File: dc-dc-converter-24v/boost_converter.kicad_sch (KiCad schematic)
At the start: 44 parts, among them Q1 SQJA42EP, Q2 SQJA42EP, Q3 SQJA42EP, Q4 SQJA42EP, U1 LM5176

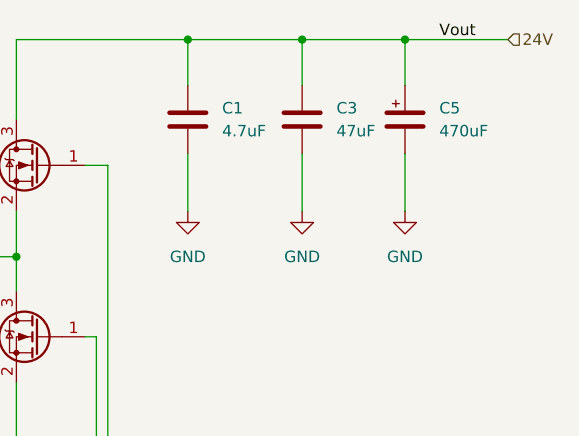
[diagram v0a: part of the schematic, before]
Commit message: improve output filter of DC-DC converter
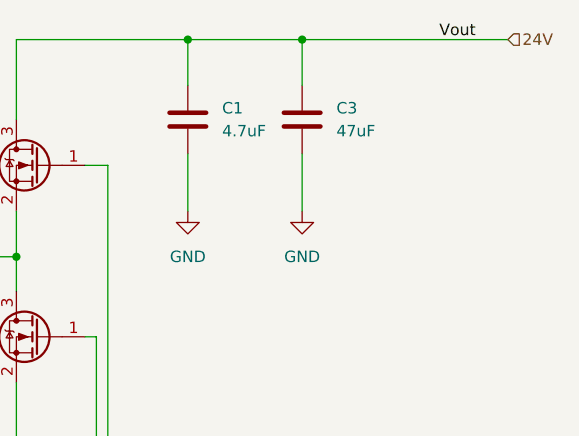
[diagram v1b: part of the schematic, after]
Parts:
- removed C5: 470uF, symbol benediktibk:C_470uF_SMD_63V_20%
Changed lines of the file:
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@@
   (junction (at 191.77 93.98) (diameter 0) (color 0 0 0 0)
   )
-  (junction (at 262.89 33.02) (diameter 0) (color 0 0 0 0)
-  )
   (junction (at 238.76 33.02) (diameter 0) (color 0 0 0 0)
   )
@@
     (stroke (width 0) (type default))
   )
-  (wire (pts (xy 262.89 45.72) (xy 262.89 52.07))
-    (stroke (width 0) (type default))
-  )
   (wire (pts (xy 191.77 52.07) (xy 191.77 57.15))
     (stroke (width 0) (type default))
@@
     (stroke (width 0) (type default))
   )
-  (wire (pts (xy 262.89 33.02) (xy 262.89 38.1))
-    (stroke (width 0) (type default))
-  )
   (wire (pts (xy 102.87 111.76) (xy 102.87 110.49))
     (stroke (width 0) (type default))
@@
     (stroke (width 0) (type default))
   )
-  (wire (pts (xy 262.89 33.02) (xy 251.46 33.02))
+  (wire (pts (xy 251.46 33.02) (xy 274.32 33.02))
     (stroke (width 0) (type default))
   )
@@
   )
   (wire (pts (xy 191.77 57.15) (xy 191.77 60.96))
-    (stroke (width 0) (type default))
-  )
-  (wire (pts (xy 274.32 33.02) (xy 262.89 33.02))
     (stroke (width 0) (type default))
   )
@@
         (path "/f3858519-f688-4645-91dc-9843c9d0ed53/67b0f940-ee28-426e-86d0-0e12eee6baf8"
           (reference "D1") (unit 1)
-        )
-      )
-    )
-  )
-  (symbol (lib_id "power:GND") (at 262.89 52.07 0) (unit 1)
-    (in_bom yes) (on_board yes) (dnp no) (fields_autoplaced)
-    (property "Reference" "#PWR05" (at 262.89 58.42 0)
-      (effects (font (size 1.27 1.27)) hide)
-    )
-    (property "Value" "GND" (at 262.89 57.15 0)
-      (effects (font (size 1.27 1.27)))
-    )
-    (property "Footprint" "" (at 262.89 52.07 0)
-      (effects (font (size 1.27 1.27)) hide)
-    )
-    (property "Datasheet" "" (at 262.89 52.07 0)
-      (effects (font (size 1.27 1.27)) hide)
-    )
-    (pin "1")
-    (instances
-      (project "dc-dc-converter-24v"
-        (path "/f3858519-f688-4645-91dc-9843c9d0ed53/67b0f940-ee28-426e-86d0-0e12eee6baf8"
-          (reference "#PWR05") (unit 1)
         )
       )
@@
         )
       )
-    )
-  )
-  (symbol (lib_id "benediktibk:C_470uF_SMD_63V_20%") (at 262.89 41.91 0) (unit 1)
-    (in_bom yes) (on_board yes) (dnp no) (fields_autoplaced)
-    (property "Reference" "C5" (at 266.7 40.64 0)
-      (effects (font (size 1.27 1.27)) (justify left))
-    )
-    (property "Value" "470uF" (at 266.7 43.18 0)
-      (effects (font (size 1.27 1.27)) (justify left))
-    )
-    (property "Footprint" "" (at 263.8552 45.72 0)
-      (effects (font (size 1.27 1.27)) hide)
-    )
-    (property "Datasheet" "~" (at 262.89 41.91 0)
-      (effects (font (size 1.27 1.27)) hide)
-    )
-    (property "RS order number" "243-7225" (at 280.416 40.64 0)
-      (effects (font (size 1.27 1.27)) hide)
-    )
-    (pin "1")
-    (pin "2")
-    (instances
-      (project "dc-dc-converter-24v"
-        (path "/f3858519-f688-4645-91dc-9843c9d0ed53/67b0f940-ee28-426e-86d0-0e12eee6baf8"
-          (reference "C5") (unit 1)
-        )
-      )

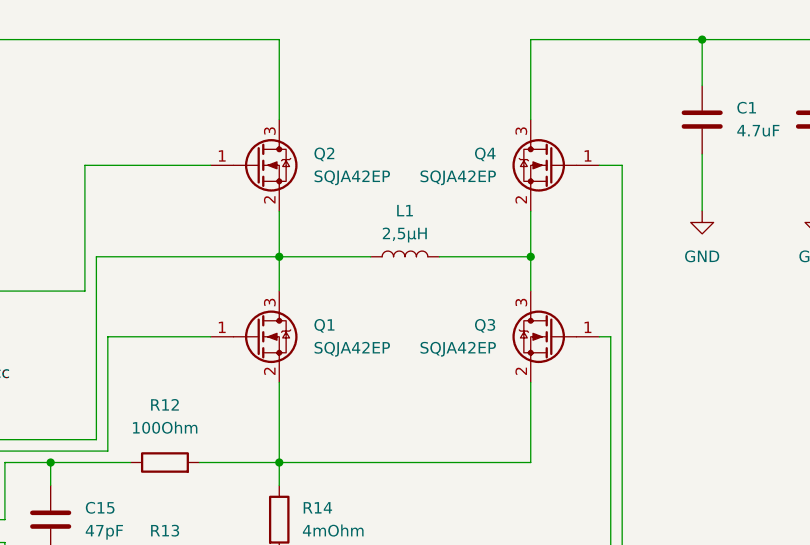
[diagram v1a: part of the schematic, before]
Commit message: update symbols and footprints
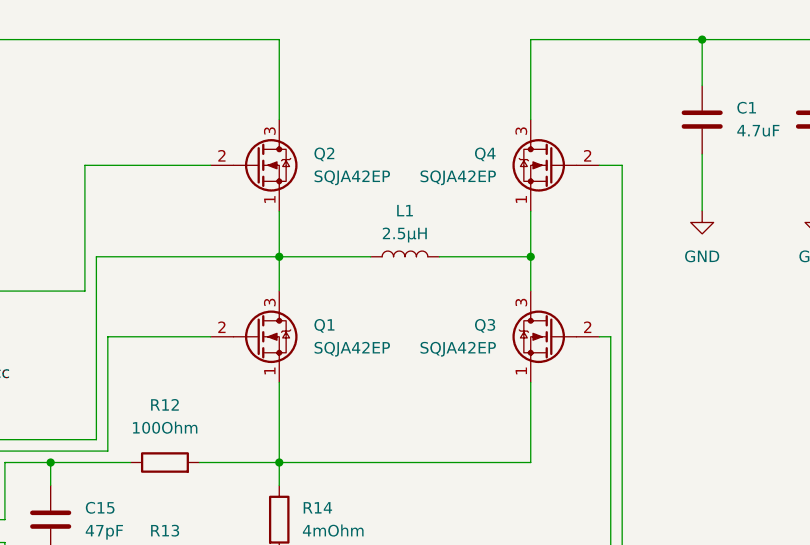
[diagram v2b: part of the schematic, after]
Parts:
- L1: value 2,5µH -> 2.5µH; footprint (none) -> benediktibk:ETQP8
- Q1, Q2, Q3, Q4: footprint (none) -> benediktibk:SQJA42EPT1_GE3
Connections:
- net at C11.2, L1.1, Q1.3 (D)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: now also Q2.1 (S); no longer Q2.2 (S)
- net at L1.2, Q3.3 (D): now also Q4.1 (S); no longer Q4.2 (S)
- net at C12.2, U1.18 (SW2): now also Q3.2 (G); no longer Q3.1 (G)
- net at R12.2, R14.1: now also Q1.1 (S), Q3.1 (S); no longer Q1.2 (S), Q3.2 (S)
- net at U1.19 (HDRV2): now also Q4.2 (G); no longer Q4.1 (G)
- net at U1.27 (HDRV1): now also Q2.2 (G); no longer Q2.1 (G)
- net at U1.25 (LDRV1): now also Q1.2 (G); no longer Q1.1 (G)
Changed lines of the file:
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@@
       (effects (font (size 1.27 1.27)))
     )
-    (property "Value" "2,5µH" (at 205.74 54.61 90)
-      (effects (font (size 1.27 1.27)))
-    )
-    (property "Footprint" "" (at 205.74 57.15 0)
+    (property "Value" "2.5µH" (at 205.74 54.61 90)
+      (effects (font (size 1.27 1.27)))
+    )
+    (property "Footprint" "benediktibk:ETQP8" (at 205.74 57.15 0)
       (effects (font (size 1.27 1.27)) hide)
     )
@@
       (effects (font (size 1.27 1.27)) (justify left))
     )
-    (property "Footprint" "" (at 217.17 63.5 0)
+    (property "Footprint" "benediktibk:SQJA42EPT1_GE3" (at 217.17 63.5 0)
       (effects (font (size 1.27 1.27)) hide)
     )
@@
       (effects (font (size 1.27 1.27)) (justify left))
     )
-    (property "Footprint" "" (at 217.17 44.45 0)
+    (property "Footprint" "benediktibk:SQJA42EPT1_GE3" (at 217.17 44.45 0)
       (effects (font (size 1.27 1.27)) hide)
     )
@@
       (effects (font (size 1.27 1.27)) (justify left))
     )
-    (property "Footprint" "" (at 194.31 44.45 0)
+    (property "Footprint" "benediktibk:SQJA42EPT1_GE3" (at 194.31 44.45 0)
       (effects (font (size 1.27 1.27)) hide)
     )
@@
       (effects (font (size 1.27 1.27)) (justify left))
     )
-    (property "Footprint" "" (at 194.31 63.5 0)
-      (effects (font (size 1.27 1.27)) hide)
-    )
+    (property "Footprint" "benediktibk:SQJA42EPT1_GE3" (at 194.31 63.5 0)
+      (effects (font (size 1.27 1.27)) hide)
+    )
